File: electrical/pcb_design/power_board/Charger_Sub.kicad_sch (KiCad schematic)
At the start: 25 parts

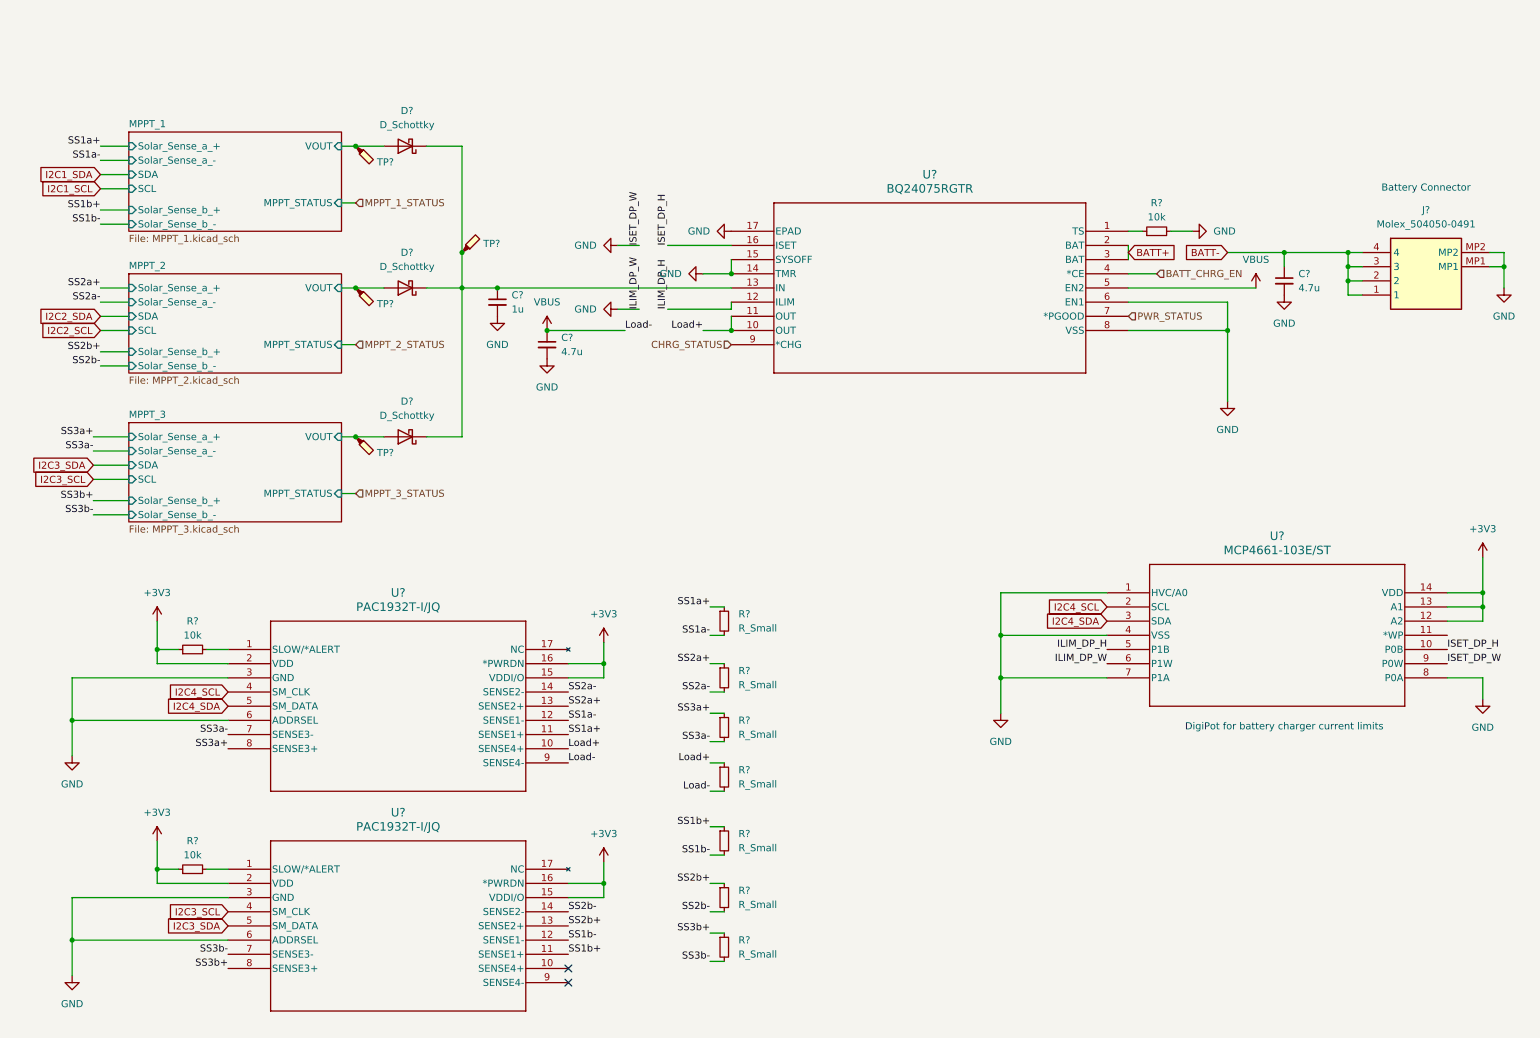
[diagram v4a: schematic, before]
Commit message: start solar connector rework
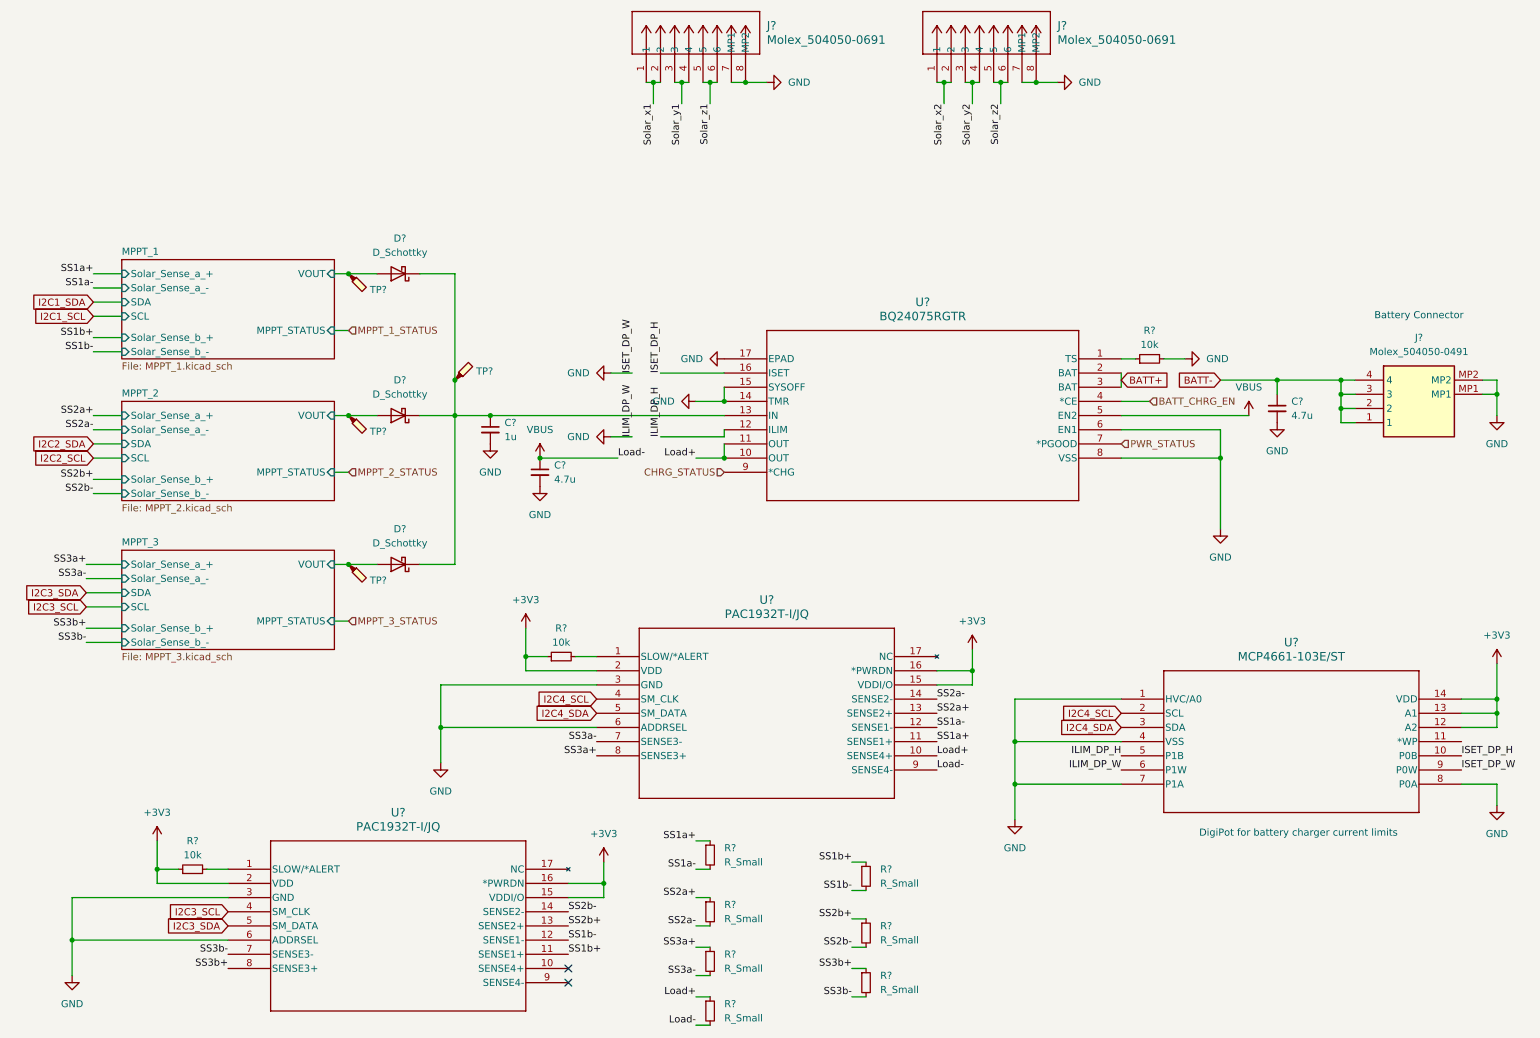
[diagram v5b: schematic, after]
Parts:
- added J? (x2): Molex_504050-0691, footprints:Molex_504050-0691, symbol tvsc_symbols:Molex_504050-0691
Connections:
- net GND: now also J?.7 (MP1), J?.7 (MP1), J?.8 (MP2), J?.8 (MP2)
- new net Solar_x1: J?.1, J?.2
- new net Solar_x2: J?.1, J?.2
- new net Solar_y1: J?.3, J?.4
- new net Solar_y2: J?.3, J?.4
- new net Solar_z1: J?.5, J?.6
- new net Solar_z2: J?.5, J?.6
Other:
- moved on the sheet: C?, D?, J?, R?, TP?, U?
